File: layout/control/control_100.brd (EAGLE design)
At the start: 100 x 42 mm, 66 parts, among them IC1 STM32F103C8T, IC2 LP2985-SOT23-5, IC3 IC_USBLC6-2, IC4 IC_USBLC6-2, IC5 LT1619ES8, IC6 LP2985-SOT23-5, IC7 IRF7470, T1 LPISR, Y1 532-CRYSTAL, Y2 EQ161-CRYSTAL

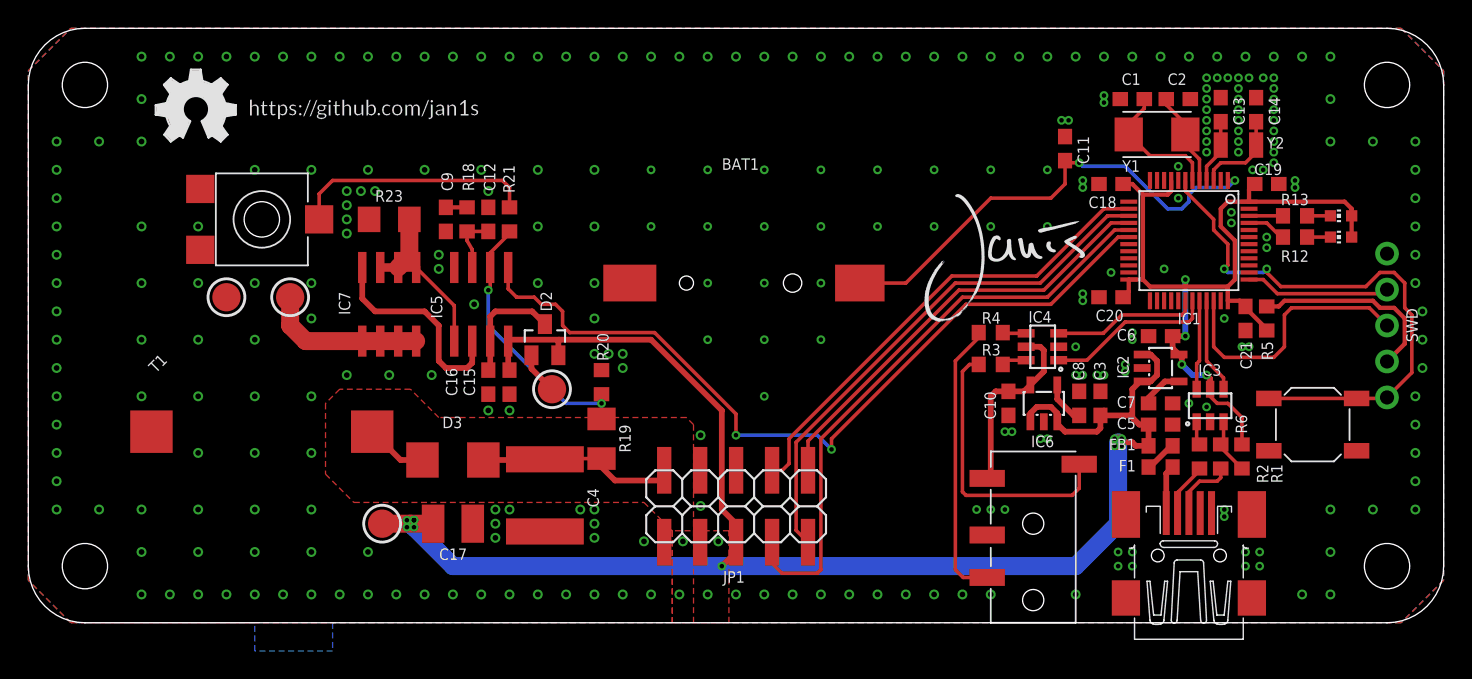
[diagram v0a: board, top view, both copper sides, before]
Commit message: Changed structure, added HM-11
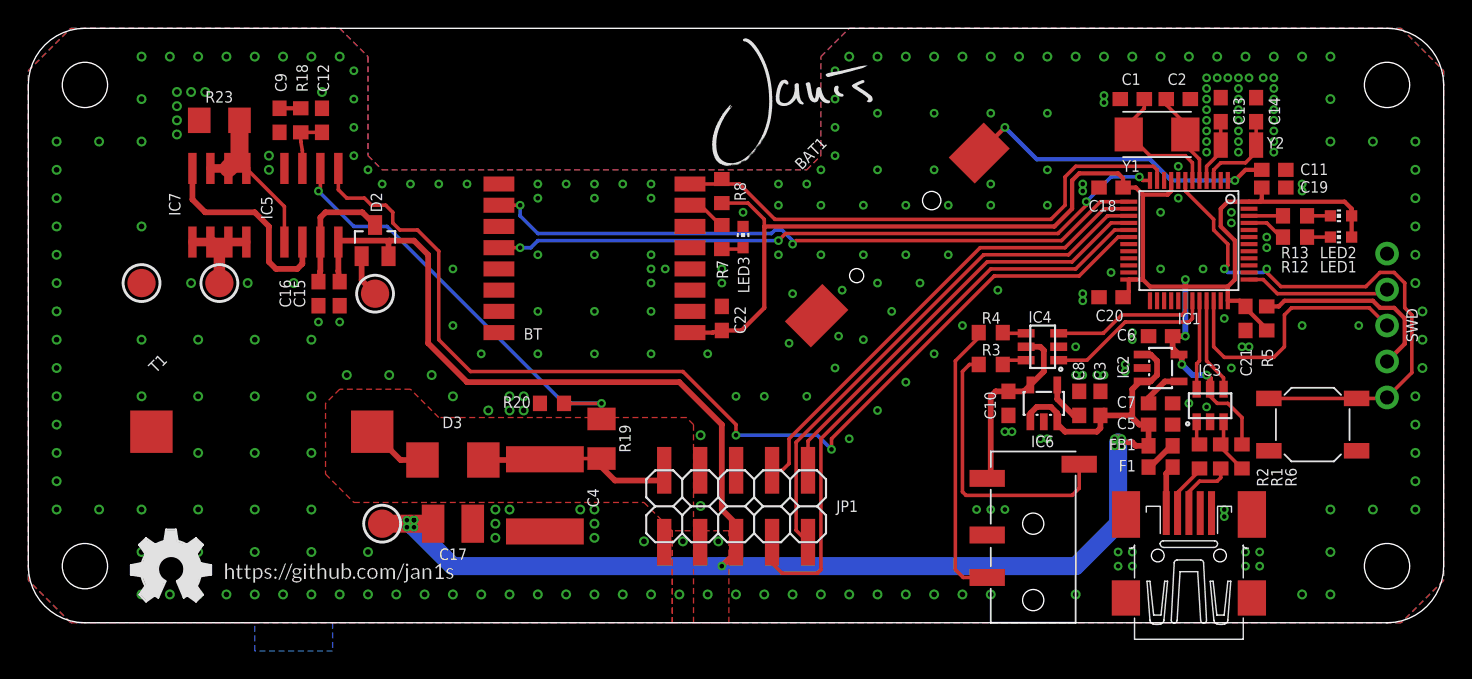
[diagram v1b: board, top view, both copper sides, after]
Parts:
- removed R21: 10k (NP), rcl:R0603
- removed R22: CA6_VSMD 10k (NP), acp:CA6-VSMD
- added BT: HM-11, bt:HM-11
- added C22: 10µF, rcl:C0603
- added LED3: (no value), led:CHIP-LED0603
- added R7: 1k, rcl:R0603
- added R8: 10k, rcl:R0603
- moved U$5 32.8 mm to (13.8, 3.00)
- moved LOGO1 32.5 mm to (7.25, 1.50)
- moved U$1 18.6 mm to (48.0, 32.0)
- moved C11 14.8 mm to (88.0, 32.0), turned to 0 degrees
- moved TP3 14.2 mm to (24.5, 23.2)
- moved D2 13.9 mm to (24.5, 27.0)
- moved IC5 13.9 mm to (20.0, 29.5)
- moved IC7 13.9 mm to (13.5, 29.5)
- moved R23 13.9 mm to (13.5, 35.5)
- moved C12 13.7 mm to (20.8, 35.5)
- moved C9 13.7 mm to (17.8, 35.5)
- moved R18 13.7 mm to (19.2, 35.5)
- moved C15 13.5 mm to (22.0, 23.2)
- moved C16 13.5 mm to (20.5, 23.2)
- moved BAT1 11.4 mm to (61.0, 27.0), turned to 135 degrees
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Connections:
- removed net N$21: R21.1, R22.B
- new net BT_USER: BT.16, IC1.11, R8.2
- new net N$26: BT.15, R7.1
- new net N$27: LED3.A, R7.2
- net +3V3: now also BT.9, C22.1, R8.1
- net GND: now also BT.12, C22.2, LED3.C; no longer R22.A
- net N$17: no longer R21.2
- net USART2_RX: now also BT.2
- net USART2_TX: now also BT.4
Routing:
- net USART2_TX: track 0.00 -> 48.3 mm, vias 0 -> 4
- net USART2_RX: track 0.00 -> 47.7 mm, vias 0 -> 2
- net +3V3: track 59.2 -> 103.3 mm
- net BT_USER: track 0.00 -> 38.1 mm
- net +5V: track 120.1 -> 138.7 mm
- net HV_EN: track 58.2 -> 76.1 mm
- net N$21: track 17.3 -> 0.00 mm
- net N$17: track 19.3 -> 34.1 mm
- net VBAT: track 34.6 -> 23.1 mm
- net N$13: track 12.8 -> 7.44 mm
- net N$26: track 0.00 -> 2.83 mm
- net N$27: track 0.00 -> 1.54 mm
- net N$19: track 8.31 -> 8.94 mm
